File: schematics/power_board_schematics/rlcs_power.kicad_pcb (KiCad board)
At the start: 2 copper layers, 45 x 75 mm, 61 parts, among them J1 SD_Card, J2 Battery Conn, J3 CONN_01X02, J4 CONN_01X02, J5 CONN_01X02, J6 CONN_01X02, J7 CONN_01X16, Q1 BSS138, Q2 BSS138, Q3 BSS138, Q4 Q_NPN_BEC, Q5 Q_NPN_BEC, T1 12 to 3v3, T2 12 to 5, T3 12-15v

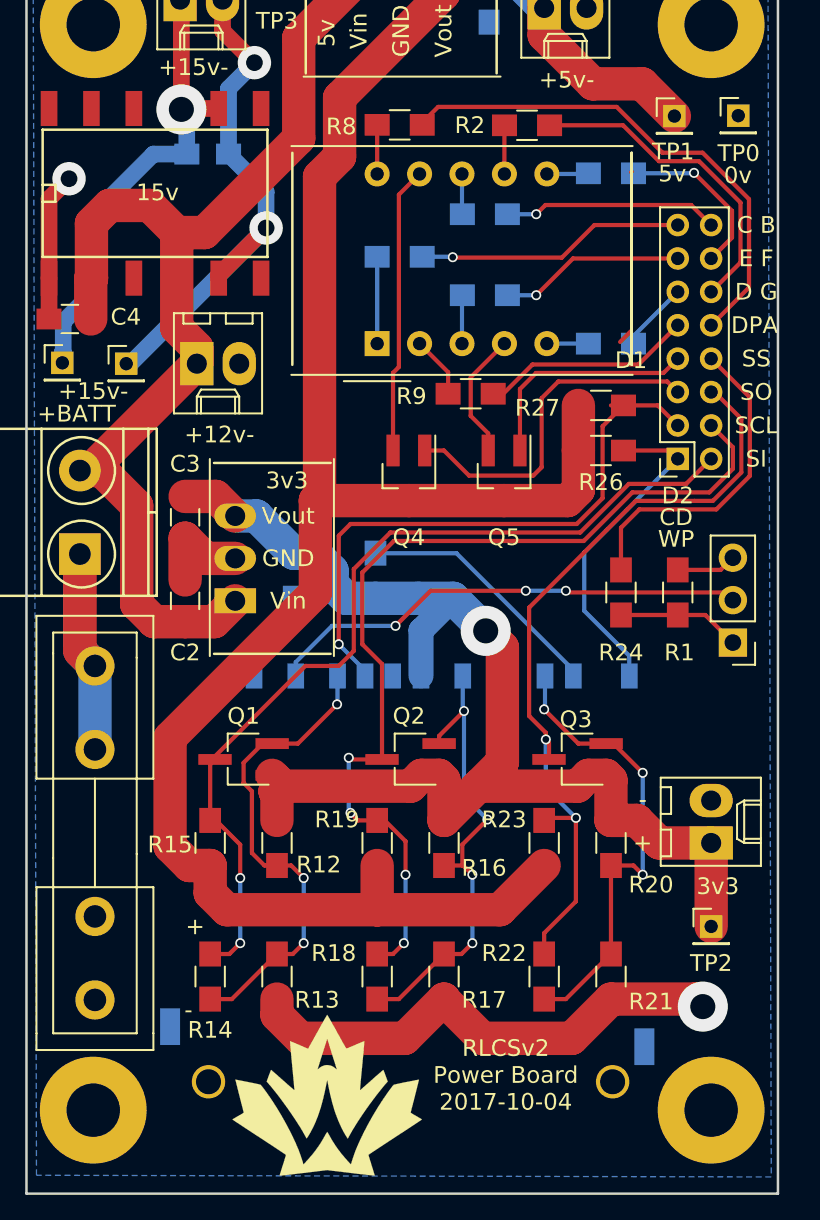
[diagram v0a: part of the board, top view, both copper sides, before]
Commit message: Change Power board Arduino connector
Also, the 15v power regulator no longer shorts its NC pins to ground
(this isn't changed in this commit, it was changed before these
schematics were added to github).
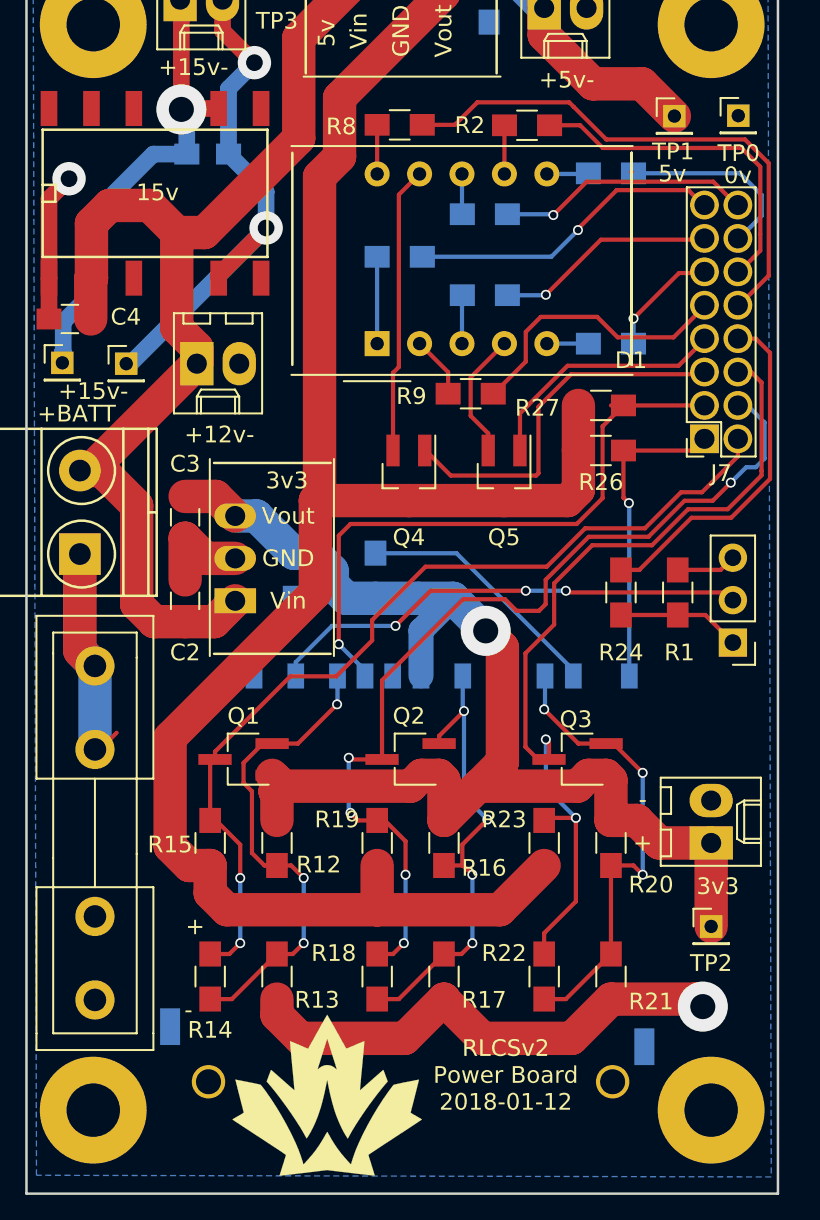
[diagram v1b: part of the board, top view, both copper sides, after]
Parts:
- moved J7 2.00 mm to (140.6, 104.8)
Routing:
- net ARD_CON_7SEG_DP: track 12.7 -> 17.5 mm
- net ARD_CON_SD_MISO: track 48.5 -> 53.0 mm
- net ARD_CON_7SEG_C: track 16.1 -> 19.1 mm
- net ARD_CON_7SEG_D: track 4.69 -> 7.33 mm, vias 0 -> 1
- net ARD_CON_7SEG_B: track 12.9 -> 15.3 mm
- net ARD_CON_7SEG_E: track 11.1 -> 13.2 mm
- net ARD_CON_SD_SS: track 19.5 -> 21.0 mm
- net ARD_CON_7SEG_D2: track 20.8 -> 22.2 mm
- net ARD_CON_7SEG_A: track 30.9 -> 32.3 mm
- net ARD_CON_7SEG_F: track 10.2 -> 11.5 mm, vias 1 -> 0
- net Net-(F1-Pad1): track 19.1 -> 20.4 mm
- net ARD_CON_7SEG_G: track 19.4 -> 20.6 mm
- net ARD_CON_SD_WP: track 20.2 -> 19.1 mm, vias 0 -> 1
- net ARD_CON_SD_CD: track 36.8 -> 37.9 mm
- net ARD_CON_SD_MOSI: track 54.8 -> 55.9 mm
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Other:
- board text added: "RLCSv2 Power Board 2018-01-12"
- board text removed: "C B"
- board text removed: "CD"
- board text removed: "D G"
- board text removed: "D2"
- board text removed: "DPA"
- board text removed: "E F"
- board text removed: "RLCSv2 Power Board 2017-10-04"
- board text removed: "SCL"
- board text removed: "SI"
- board text removed: "SO"
- board text removed: "SS"
- board text removed: "WP"

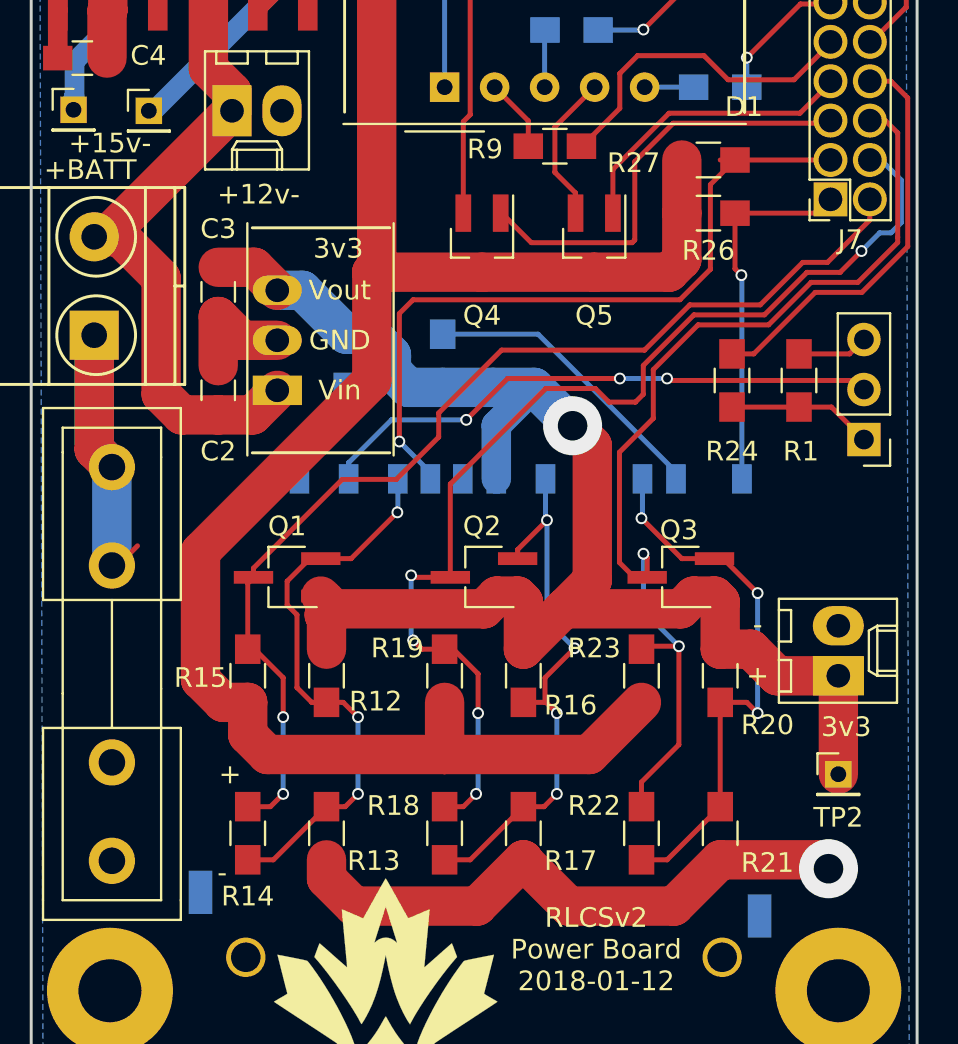
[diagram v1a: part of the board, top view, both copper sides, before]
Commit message: Replace bidirectional shifter for SD card
Now MOSI and SCL run through voltage dividers, and MISO is just a wire.
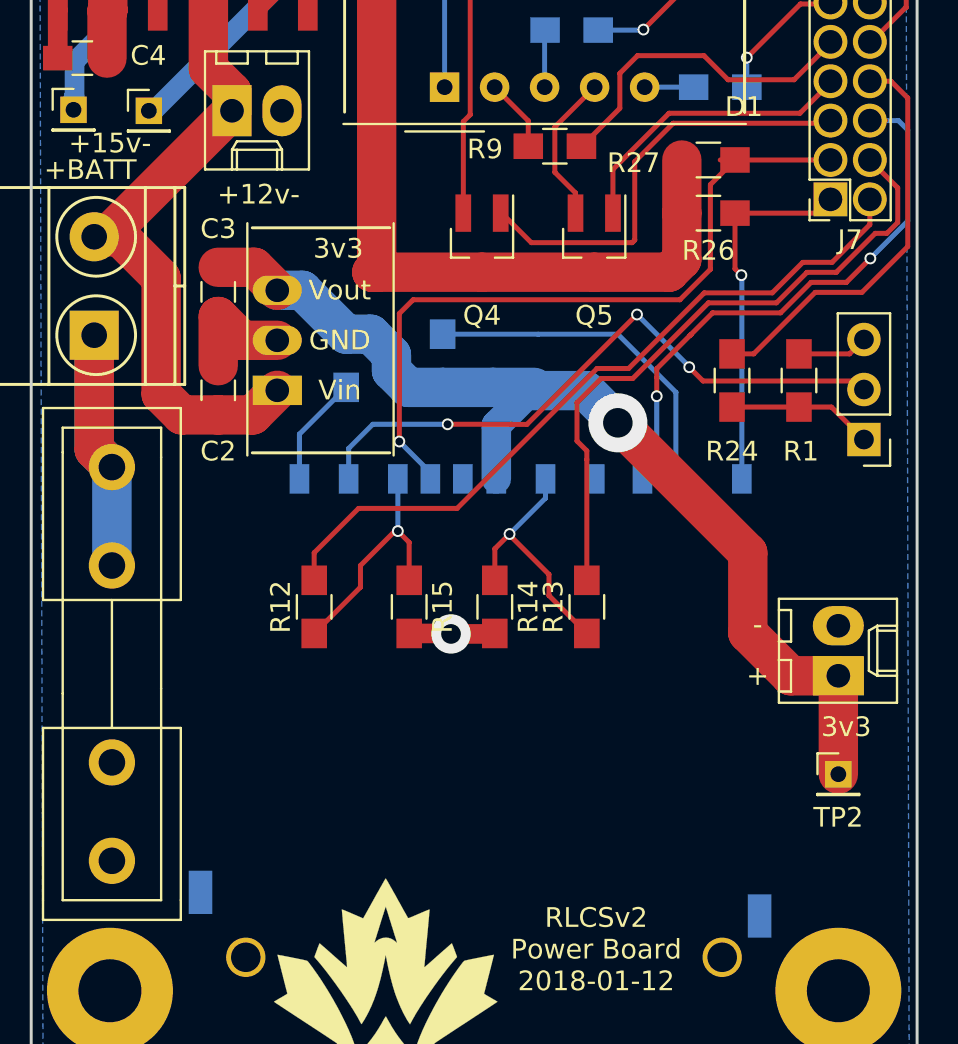
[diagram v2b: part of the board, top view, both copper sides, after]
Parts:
- removed Q1, Q2, Q3: BSS138, TO_SOT_Packages_SMD:TSOT-23_HandSoldering
- removed R16, R18, R19, R20, R22, R23: 10K, Resistors_SMD:R_0805_HandSoldering
- removed R17, R21: 20K, Resistors_SMD:R_0805_HandSoldering
- R13: value 20K -> 10K
- R14, R15: value 10K -> 20K
- moved R13 17.5 mm to (128.2, 125.5)
- moved R14 17.0 mm to (123.5, 125.5)
- moved R15 8.92 mm to (119.2, 125.5), turned to 270 degrees
- moved R12 3.56 mm to (114.4, 125.5), turned to 90 degrees
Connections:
- J1 pad 2: /MOSI/3v3side -> Net-(J1-Pad2)
- J1 pad 5: /SCL/3v3side -> Net-(J1-Pad5)
- J1 pad 7: /MISO/3v3side -> ARD_CON_SD_MISO
- R12 pad 1: +3V3 -> Net-(J1-Pad2)
- R12 pad 2: /MOSI/3v3side -> ARD_CON_SD_MOSI
- R13 pad 1: GND -> Net-(J1-Pad5)
- R13 pad 2: /MOSI/3v3side -> ARD_CON_SD_SCL
- R14 pad 1: ARD_CON_SD_MOSI -> Net-(J1-Pad5)
- R14 pad 2: /MOSI/3v3side -> GND
- R15 pad 1: +5V -> Net-(J1-Pad2)
- R15 pad 2: ARD_CON_SD_MOSI -> GND
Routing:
- net +5V: track 127.1 -> 74.1 mm
- net /MOSI/3v3side: track 29.0 -> 0.00 mm, vias 3 -> 0
- net /SCL/3v3side: track 28.3 -> 0.00 mm, vias 4 -> 0
- net /MISO/3v3side: track 28.1 -> 0.00 mm, vias 3 -> 0
- net GND: track 48.7 -> 22.9 mm
- net +3V3: track 78.9 -> 53.5 mm
- net ARD_CON_SD_MISO: track 53.0 -> 29.8 mm
- net ARD_CON_SD_SCL: track 56.1 -> 33.7 mm, vias 5 -> 0
- net ARD_CON_SD_MOSI: track 55.9 -> 39.9 mm, vias 2 -> 0
- net Net-(J1-Pad5): track 0.00 -> 12.9 mm, vias 0 -> 1
- net Net-(J1-Pad2): track 0.00 -> 12.4 mm, vias 0 -> 1
- net Net-(J1-Pad1): track 30.5 -> 34.3 mm
- net Net-(J1-Pad8): track 15.1 -> 17.8 mm
- net Net-(F1-Pad1): track 20.4 -> 19.1 mm

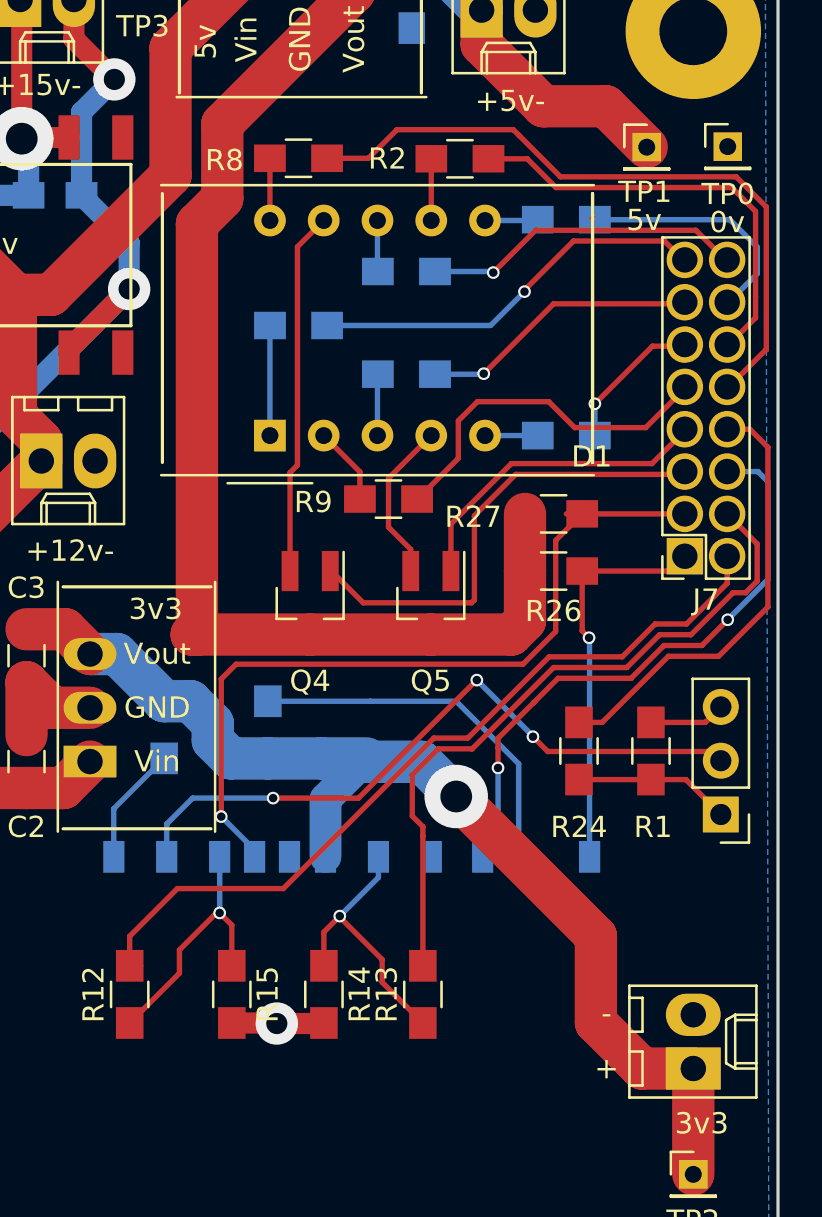
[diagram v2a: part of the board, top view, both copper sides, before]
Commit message: Actually make it a 2.54mm pitch connector
whoops, I had a 2mm pitch one, now it's fixed and is proper. DRC passes
with flying colours.
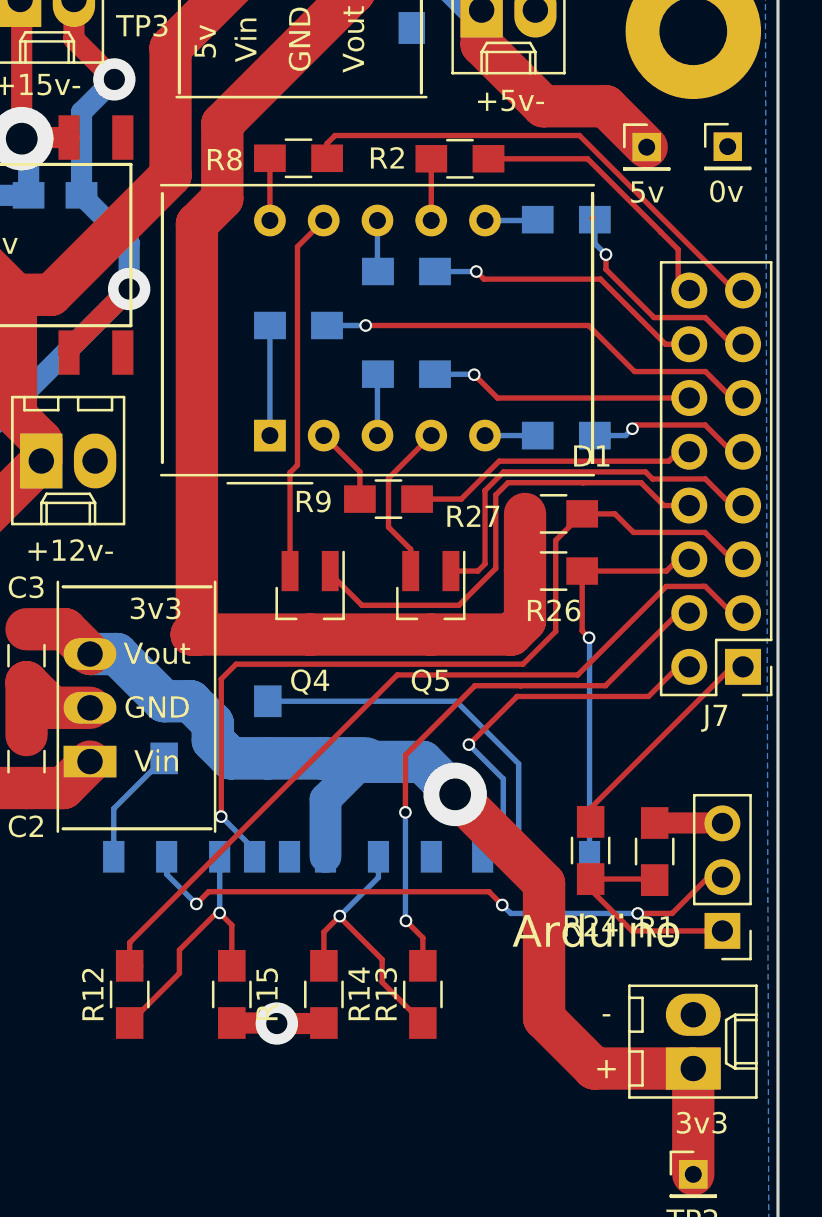
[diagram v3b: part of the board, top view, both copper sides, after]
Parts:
- J7: footprint Socket_Strips:Socket_Strip_Straight_2x08_Pitch2.00mm -> Pin_Headers:Pin_Header_Straight_2x08_Pitch2.54mm
- moved J7 5.90 mm to (143.3, 110.0)
- moved JP1 5.50 mm to (142.4, 122.5)
- moved R1 4.75 mm to (139.2, 118.8)
- moved R24 4.73 mm to (136.2, 118.7)
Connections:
- J7 pad 1: ARD_CON_SD_WP -> ARD_CON_SD_SS
- J7 pad 10: ARD_CON_7SEG_A -> ARD_CON_7SEG_DP
- J7 pad 11: ARD_CON_7SEG_D -> ARD_CON_7SEG_C
- J7 pad 12: ARD_CON_7SEG_G -> ARD_CON_7SEG_E
- J7 pad 13: ARD_CON_7SEG_E -> ARD_CON_7SEG_F
- J7 pad 14: ARD_CON_7SEG_F -> ARD_CON_7SEG_B
- J7 pad 15: ARD_CON_7SEG_C -> ARD_CON_7SEG_A
- J7 pad 16: ARD_CON_7SEG_B -> ARD_CON_7SEG_G
- J7 pad 2: ARD_CON_SD_MOSI -> ARD_CON_SD_MISO
- J7 pad 3: ARD_CON_SD_CD -> ARD_CON_SD_MOSI
- J7 pad 5: ARD_CON_7SEG_D2 -> ARD_CON_SD_CD
- J7 pad 6: ARD_CON_SD_MISO -> ARD_CON_SD_WP
- J7 pad 8: ARD_CON_SD_SS -> ARD_CON_7SEG_D2
- J7 pad 9: ARD_CON_7SEG_DP -> ARD_CON_7SEG_D
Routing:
- net ARD_CON_SD_MISO: track 29.8 -> 18.2 mm, vias 2 -> 1
- net ARD_CON_SD_SS: track 21.0 -> 10.1 mm
- net ARD_CON_7SEG_A: track 32.3 -> 24.0 mm
- net ARD_CON_7SEG_G: track 20.6 -> 12.7 mm
- net ARD_CON_SD_SCL: track 33.7 -> 26.0 mm, vias 0 -> 2
- net Net-(J1-Pad1): track 34.3 -> 29.4 mm
- net ARD_CON_7SEG_DP: track 17.5 -> 13.9 mm
- net Net-(JP1-Pad1): track 7.38 -> 10.6 mm
- net ARD_CON_7SEG_D1: track 15.1 -> 17.9 mm
- net ARD_CON_SD_CD: track 37.9 -> 40.3 mm
- net ARD_CON_7SEG_B: track 15.3 -> 12.9 mm
- net ARD_CON_SD_MOSI: track 39.9 -> 38.1 mm
- net ARD_CON_7SEG_F: track 11.5 -> 9.98 mm, vias 0 -> 1
- net ARD_CON_7SEG_C: track 19.1 -> 20.5 mm
- net +3V3: track 53.5 -> 54.8 mm
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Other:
- board text added: "Arduino"

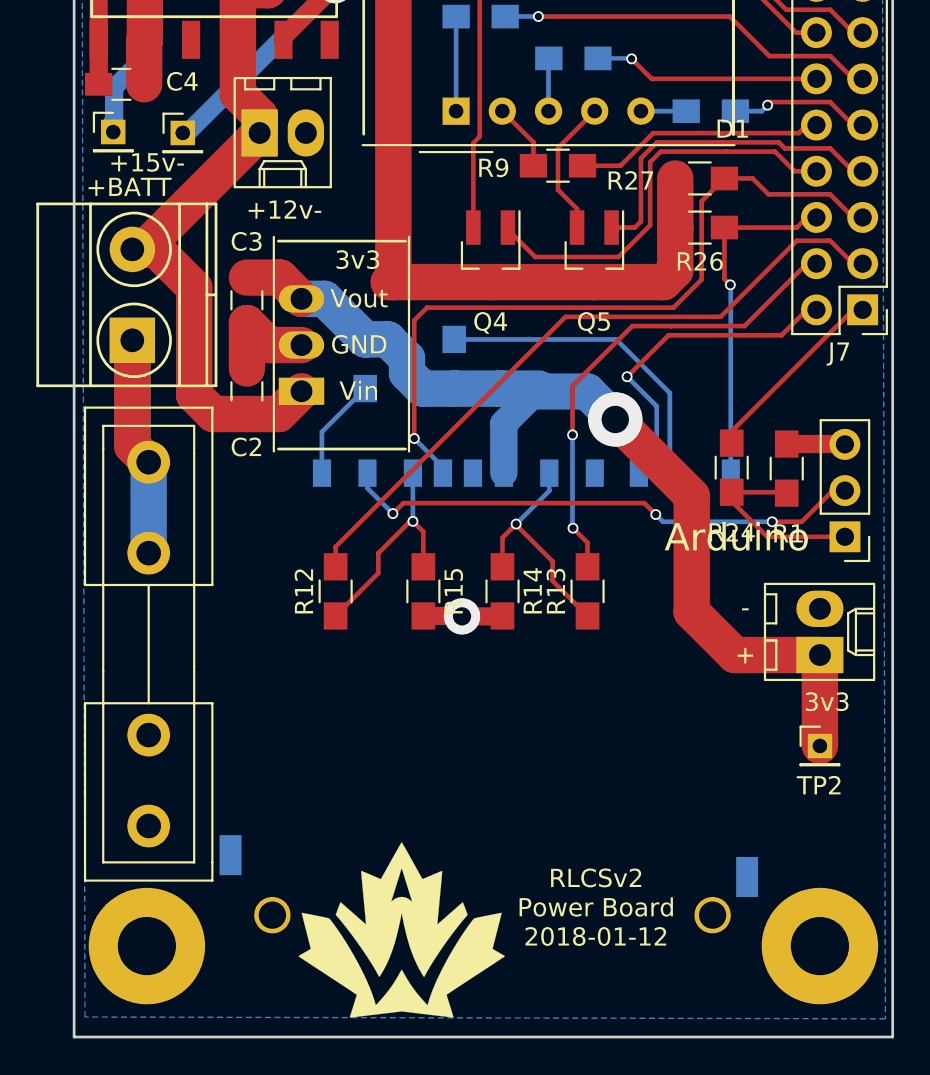
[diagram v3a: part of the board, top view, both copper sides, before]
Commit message: Silkscreen changes
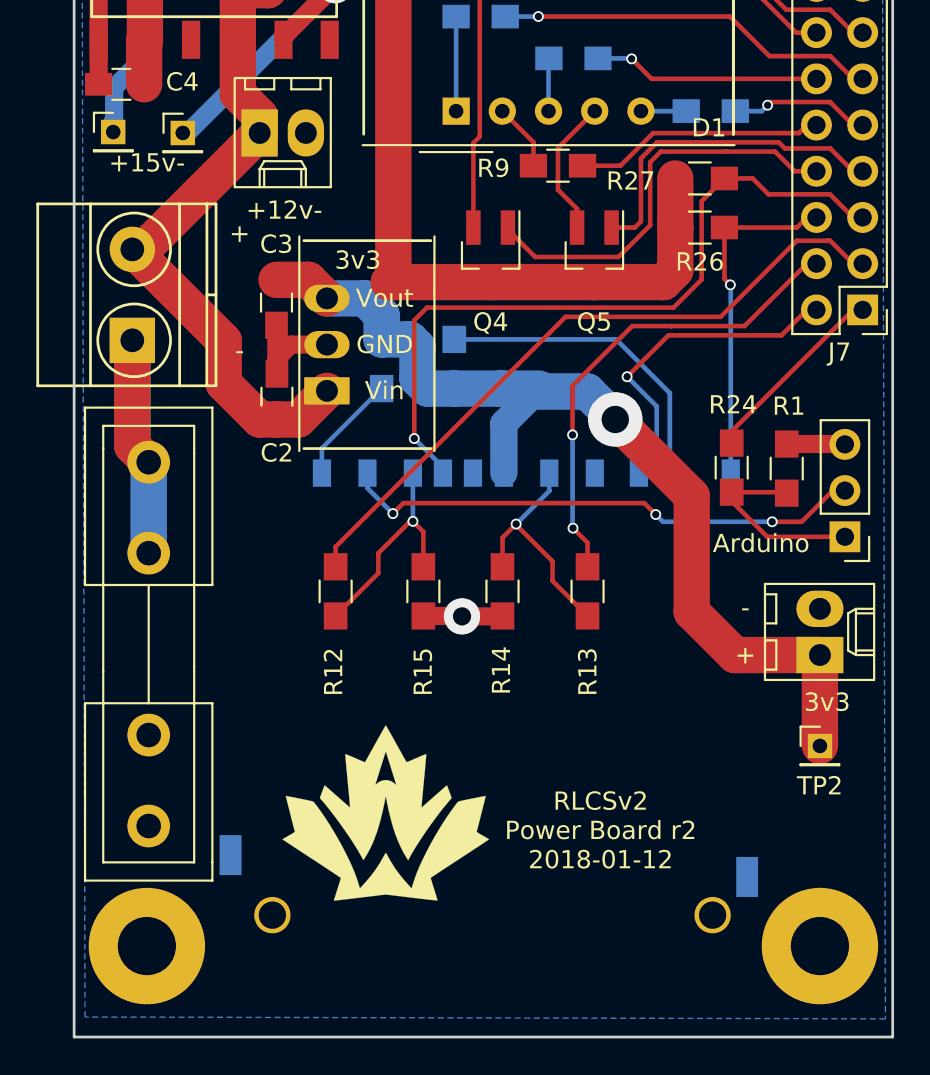
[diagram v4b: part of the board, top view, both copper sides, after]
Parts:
- moved G*** 6.48 mm to (117.1, 137.7)
- moved C2 1.68 mm to (111.2, 114.8)
- moved C3 1.63 mm to (111.1, 109.6)
- moved T1 1.40 mm to (113.9, 114.5)
- moved R11 0.90 mm to (116.9, 113.0)
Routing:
- net GND: track 22.5 -> 25.8 mm
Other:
- board text added: "+ -"
- board text added: "RLCSv2 Power Board r2 2018-01-12"
- board text removed: "+BATT"
- board text removed: "RLCSv2 Power Board 2018-01-12"

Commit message: Change fusing from bottom side to top side
Correct that error. Also add flyback diode to relay board
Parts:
- moved J2 26.6 mm to (103.4, 138.3)
- moved F1 8.45 mm to (103.4, 126.8), turned to 90 degrees
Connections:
- F1 pad 2: GND -> +12P
- J2 pad 1: Net-(F1-Pad1) -> GND
- J2 pad 2: +12P -> Net-(F1-Pad1)
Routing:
- net Net-(F1-Pad1): track 19.1 -> 16.5 mm
- net +12P: track 72.6 -> 74.5 mm
